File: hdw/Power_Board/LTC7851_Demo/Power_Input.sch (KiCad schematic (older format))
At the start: 29 parts, among them J201 +12V IN, J206 GND IN, Q201 IPC100N04S51R7ATMA1, Q202 IPC100N04S51R7ATMA1, U201 LTC4365DDB, U202 74LVC1G06

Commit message: Added to do list iem
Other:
- note added: "UVLO threshold set to 10V\nOVLO threshold set to 14V"
- moved on the sheet: ECO2
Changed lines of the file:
@@
 L Motor:Fan ECO2
 U 1 1 5BFE4F70
-P 1610 5230
-F 0 "ECO2" H 1710 5430 50  0000 L CNN
-F 1 "Fan" H 1710 5130 50  0000 L TNN
-F 2 "" H 1610 5240 50  0001 C CNN
-F 3 "~" H 1610 5240 50  0001 C CNN
-	1    1610 5230
+P 1970 6930
+F 0 "ECO2" H 2070 7130 50  0000 L CNN
+F 1 "Fan" H 2070 6830 50  0000 L TNN
+F 2 "" H 1970 6940 50  0001 C CNN
+F 3 "~" H 1970 6940 50  0001 C CNN
+	1    1970 6930
 	1    0    0    -1
 $EndComp
-NoConn ~ 1610 4930
-NoConn ~ 1610 5430
-Text Notes 880  5670 0    50   ~ 0
+NoConn ~ 1970 6630
+NoConn ~ 1970 7130
+Text Notes 1240 7370 0    50   ~ 0
 Fan added for forced air cooling
 $Comp
@@
 Text Notes 6540 6460 0    50   ~ 0
 Note: Components with 'ECO' Reference Designators are modifications to the original design
+Text Notes 1270 5160 0    50   ~ 0
+UVLO threshold set to 10V\nOVLO threshold set to 14V
 $EndSCHEMATC

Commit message: Resolved a few library dependencies
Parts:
- TP201, TP202: symbol Custom_Library:TP -> LED_Display_Local_Library:TP
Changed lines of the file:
@@
 	7750 2650 7750 2720
 $Comp
-L Custom_Library:TP TP202
+L LED_Display_Local_Library:TP TP202
 U 1 1 5BB7B6E2
 P 7000 2650
@@
 $EndComp
 $Comp
-L Custom_Library:TP TP201
+L LED_Display_Local_Library:TP TP201
 U 1 1 5BB80406
 P 1880 3880
@@
 	2840 2640 2840 2720
 $Comp
-L Custom_Library:+5.5V_MNG #PWR0210
+L LED_Display_Local_Library:+5.5V_MNG #PWR0210
 U 1 1 5BBEC090
 P 6050 4260
@@
 $EndComp
 $Comp
-L Custom_Library:+5.5V_MNG #PWR0216
+L LED_Display_Local_Library:+5.5V_MNG #PWR0216
 U 1 1 5BC2A9CC
 P 8340 5040
@@
 $EndComp
 $Comp
-L Custom_Library:+5.5V_MNG #PWR0220
+L LED_Display_Local_Library:+5.5V_MNG #PWR0220
 U 1 1 5BC2A9EC
 P 9050 4390
@@
 $EndComp
 $Comp
-L Custom_Library:+5.5V_MNG #PWR0214
+L LED_Display_Local_Library:+5.5V_MNG #PWR0214
 U 1 1 5BC2A9FE
 P 7940 5390

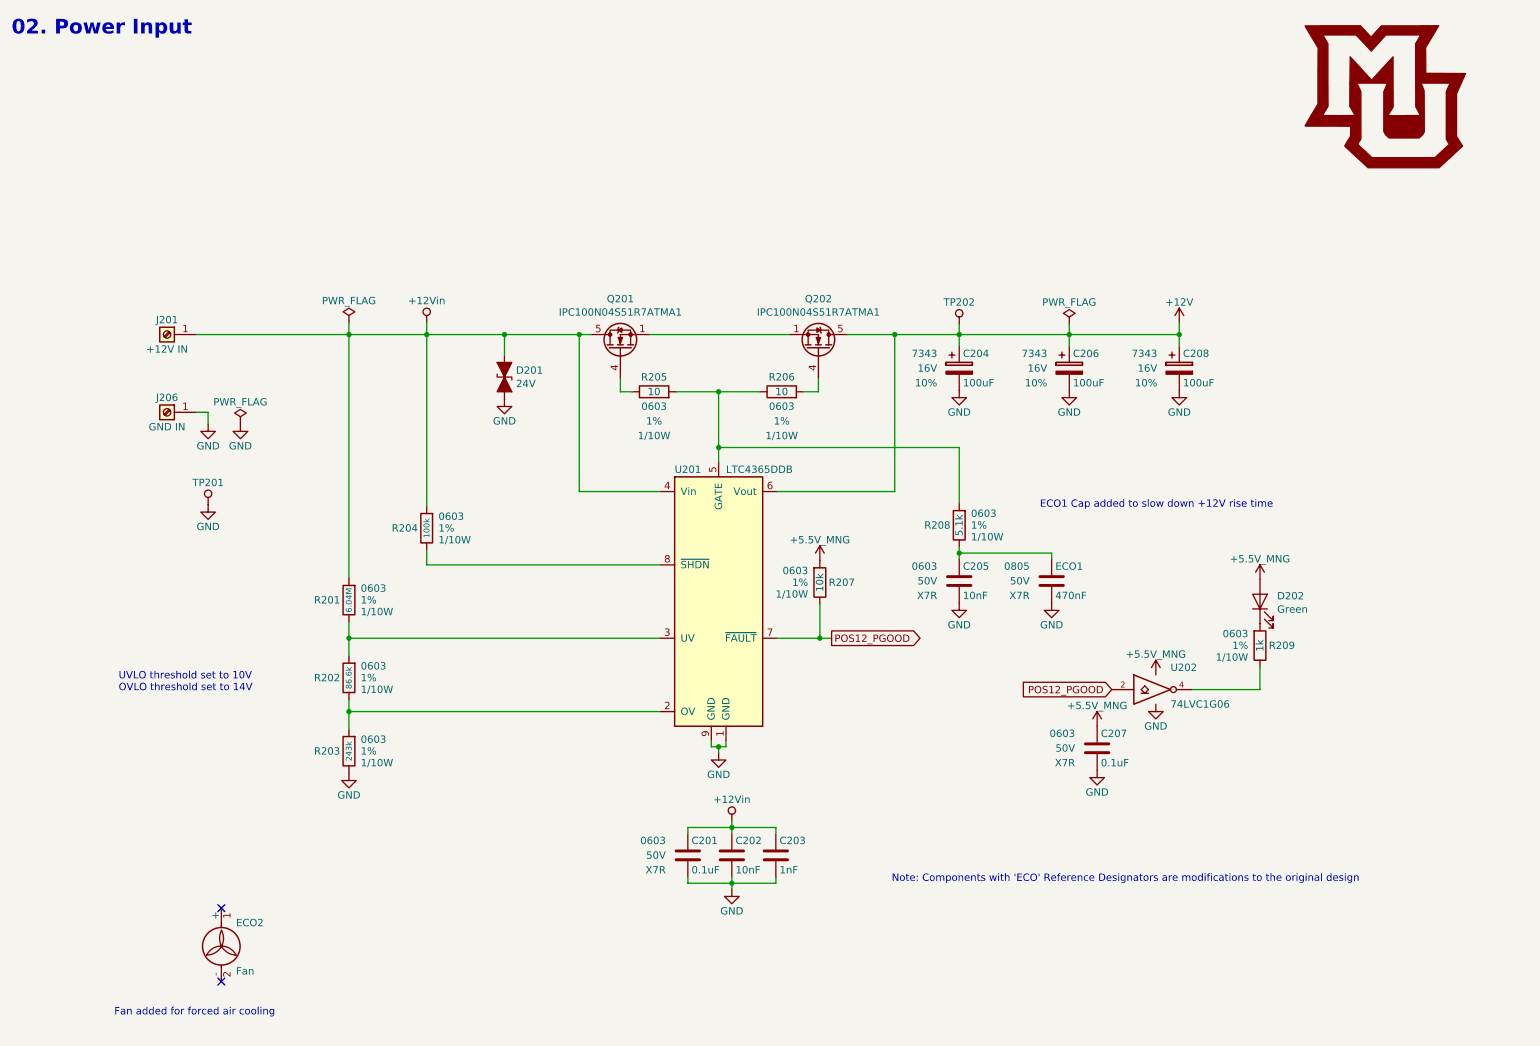
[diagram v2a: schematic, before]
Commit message: Added ECOs to hardware schematics
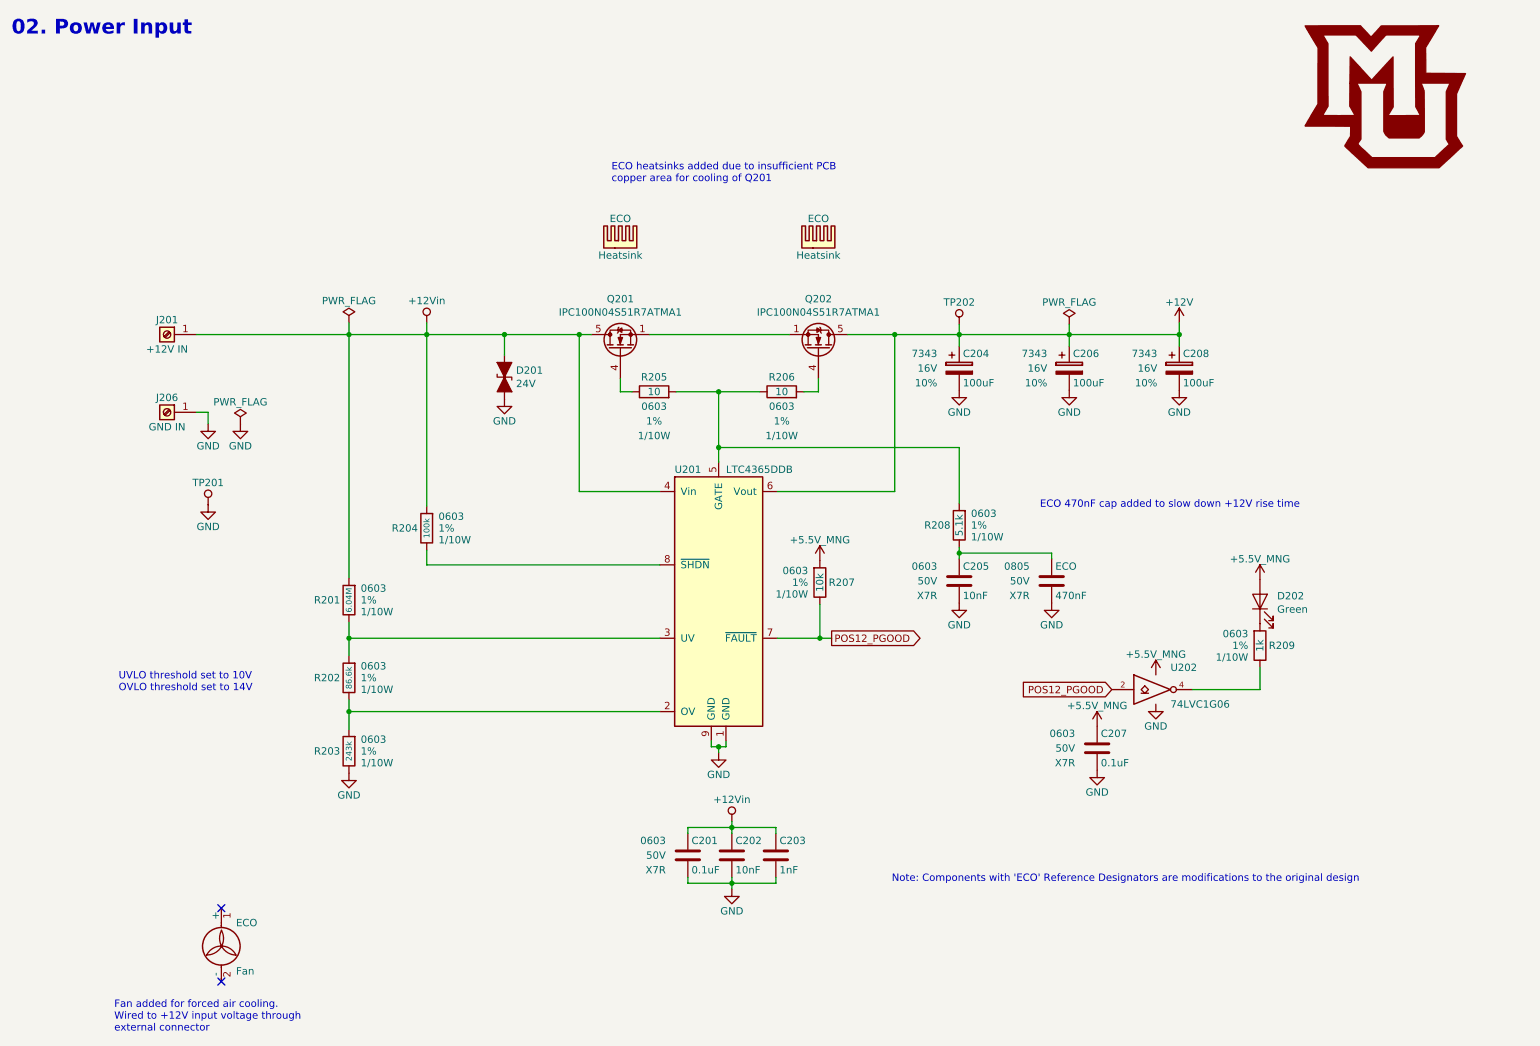
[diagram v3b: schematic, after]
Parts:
- added ECO (x2): Heatsink, symbol Mechanical:Heatsink
- renumbered ECO1 to ECO, ECO2 to ECO
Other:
- note added: "ECO 470nF cap added to slow down +12V rise time"
- note added: "ECO heatsinks added due to insufficient PCB\ncopper area for cooling of Q201"
- note added: "Fan added for forced air cooling.\nWired to +12V input voltage through\nexternal connector"
- note removed: "ECO1 Cap added to slow down +12V rise time"
- note removed: "Fan added for forced air cooling"
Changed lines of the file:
@@
 EESchema Schematic File Version 4
 LIBS:LTC7851_Demo-cache
-EELAYER 26 0
+EELAYER 29 0
 EELAYER END
 $Descr A 11000 8500
@@
 AR Path="/5BB2595E/5BFDF337" Ref="C?"  Part="1"
 AR Path="/5BAAE0FA/5BFDF337" Ref="C?"  Part="1"
-AR Path="/5BB86F23/5BFDF337" Ref="ECO1"  Part="1"
-F 0 "ECO1" H 7655 4500 50  0000 L CNN
+AR Path="/5BB86F23/5BFDF337" Ref="ECO"  Part="1"
+F 0 "ECO" H 7655 4500 50  0000 L CNN
 F 1 "470nF" H 7655 4300 50  0000 L CNN
 F 2 "" H 7668 4250 50  0001 C CNN
@@
 	7000 4210 7000 4170
 Text Notes 7550 3910 0    50   ~ 0
-ECO1 Cap added to slow down +12V rise time
-$Comp
-L Motor:Fan ECO2
+ECO 470nF cap added to slow down +12V rise time
+$Comp
+L Motor:Fan ECO
 U 1 1 5BFE4F70
 P 1970 6930
-F 0 "ECO2" H 2070 7130 50  0000 L CNN
+F 0 "ECO" H 2070 7130 50  0000 L CNN
 F 1 "Fan" H 2070 6830 50  0000 L TNN
 F 2 "" H 1970 6940 50  0001 C CNN
@@
 NoConn ~ 1970 6630
 NoConn ~ 1970 7130
-Text Notes 1240 7370 0    50   ~ 0
-Fan added for forced air cooling
+Text Notes 1240 7480 0    50   ~ 0
+Fan added for forced air cooling.\nWired to +12V input voltage through\nexternal connector
 $Comp
 L LED_Display_Local_Library:MU_Logo #G?
@@
 Text Notes 1270 5160 0    50   ~ 0
 UVLO threshold set to 10V\nOVLO threshold set to 14V
+$Comp
+L Mechanical:Heatsink ECO
+U 1 1 5CBCAE52
+P 4690 2130
+F 0 "ECO" H 4690 2330 50  0000 C CNN
+F 1 "Heatsink" H 4690 2080 50  0000 C CNN
+F 2 "" H 4702 2130 50  0001 C CNN
+F 3 "~" H 4702 2130 50  0001 C CNN
+	1    4690 2130
+	1    0    0    -1
+$EndComp
+$Comp
+L Mechanical:Heatsink ECO
+U 1 1 5CBCB0B3
+P 6040 2130
+F 0 "ECO" H 6040 2330 50  0000 C CNN
+F 1 "Heatsink" H 6040 2080 50  0000 C CNN
+F 2 "" H 6052 2130 50  0001 C CNN
+F 3 "~" H 6052 2130 50  0001 C CNN
+	1    6040 2130
+	1    0    0    -1
+$EndComp
+Text Notes 4630 1690 0    50   ~ 0
+ECO heatsinks added due to insufficient PCB\ncopper area for cooling of Q201
 $EndSCHEMATC

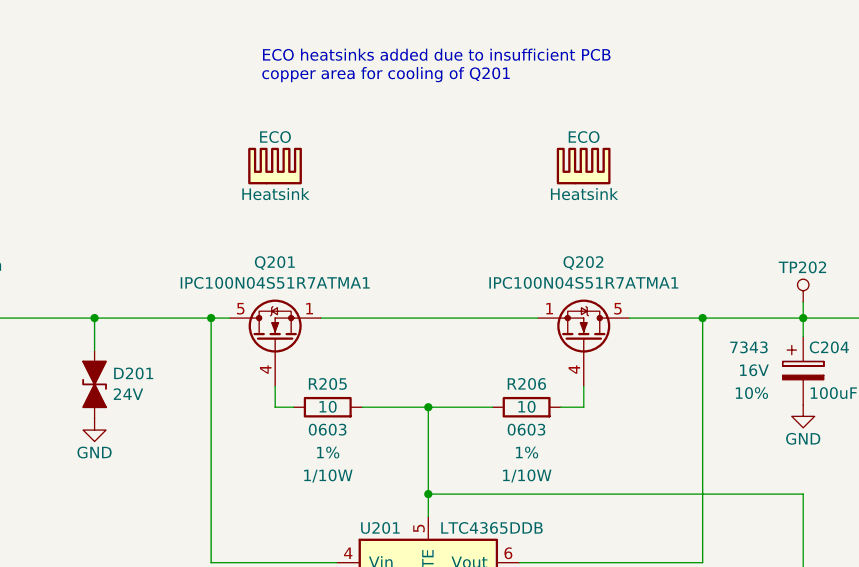
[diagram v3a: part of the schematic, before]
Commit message: Hardware changes, removed conditional USB printing
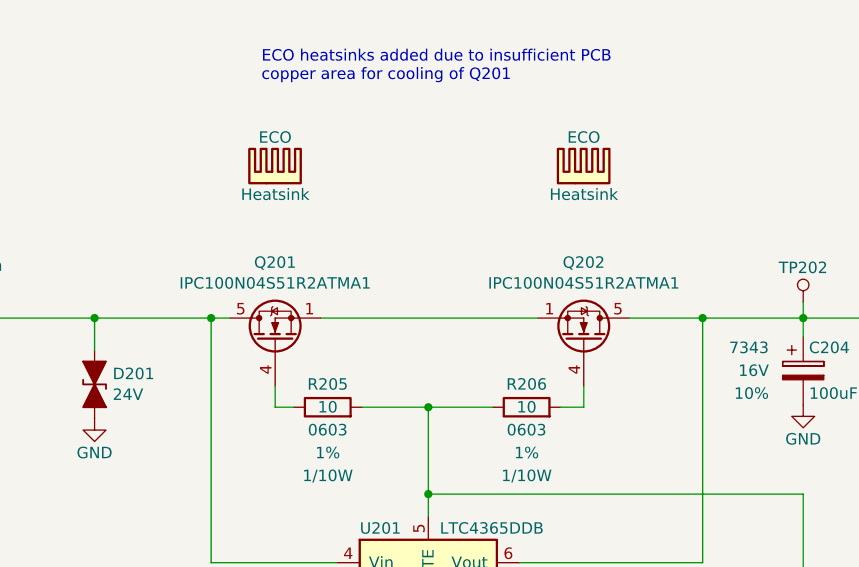
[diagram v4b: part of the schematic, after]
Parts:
- ECO: Digi-Key PN (none) -> 603-1006-ND
- Q201, Q202: value IPC100N04S51R7ATMA1 -> IPC100N04S51R2ATMA1; Digi-Key PN BSC123N10LSGATMA1CT-ND -> IPC100N04S51R2ATMA1CT-ND
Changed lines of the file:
@@
 AR Path="/5BB86F23/5BC3F351" Ref="Q201"  Part="1"
 F 0 "Q201" V 5033 2820 50  0000 C CNN
-F 1 "IPC100N04S51R7ATMA1" V 4942 2820 50  0000 C CNN
+F 1 "IPC100N04S51R2ATMA1" V 4942 2820 50  0000 C CNN
 F 2 "TO_SOT_Packages_SMD:TDSON-8-1" H 4890 2745 50  0001 L CIN
 F 3 "http://www.infineon.com/dgdl/Infineon-BSC123N10LS-DS-v02_08-en.pdf?fileId=db3a30431b3e89eb011b4626974b7df5" V 4690 2820 50  0001 L CNN
-F 4 "BSC123N10LSGATMA1CT-ND" H 4690 2820 50  0001 C CNN "Digi-Key PN"
+F 4 "IPC100N04S51R2ATMA1CT-ND" H 4690 2820 50  0001 C CNN "Digi-Key PN"
 	1    4690 2820
 	0    -1   -1   0
@@
 AR Path="/5BB86F23/5BC46F59" Ref="Q202"  Part="1"
 F 0 "Q202" V 6383 2820 50  0000 C CNN
-F 1 "IPC100N04S51R7ATMA1" V 6292 2820 50  0000 C CNN
+F 1 "IPC100N04S51R2ATMA1" V 6292 2820 50  0000 C CNN
 F 2 "TO_SOT_Packages_SMD:TDSON-8-1" H 6240 2745 50  0001 L CIN
 F 3 "http://www.infineon.com/dgdl/Infineon-BSC123N10LS-DS-v02_08-en.pdf?fileId=db3a30431b3e89eb011b4626974b7df5" V 6040 2820 50  0001 L CNN
-F 4 "BSC123N10LSGATMA1CT-ND" H 6040 2820 50  0001 C CNN "Digi-Key PN"
+F 4 "IPC100N04S51R2ATMA1CT-ND" H 6040 2820 50  0001 C CNN "Digi-Key PN"
 	1    6040 2820
 	0    1    -1   0
@@
 F 2 "" H 1970 6940 50  0001 C CNN
 F 3 "~" H 1970 6940 50  0001 C CNN
+F 4 "603-1006-ND" H 1970 6930 50  0001 C CNN "Digi-Key PN"
 	1    1970 6930
 	1    0    0    -1
